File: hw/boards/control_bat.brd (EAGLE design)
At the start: 101.6 x 30.5 mm, 18 parts, among them U1 579-MCP1703T-3002ECB, U2 771-LPC824M201JDH20J, U3 888-XB24CZ7PIS-004

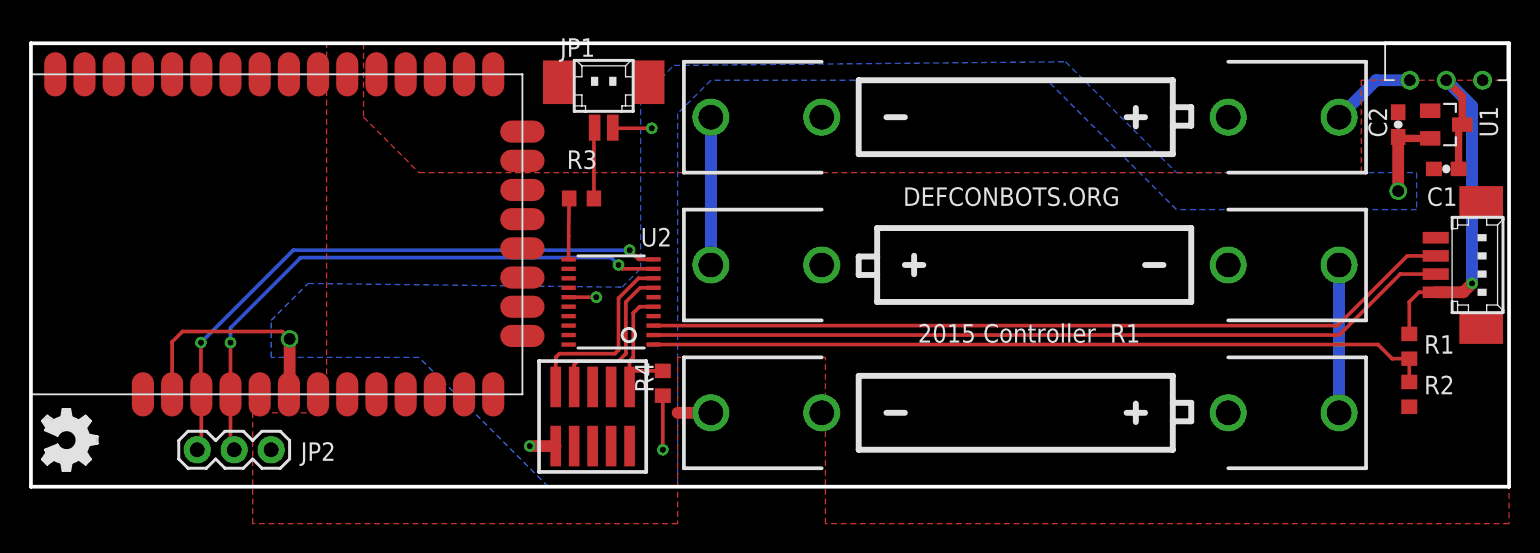
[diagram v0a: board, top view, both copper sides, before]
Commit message: Cleanup some routing. Fix some part numbers
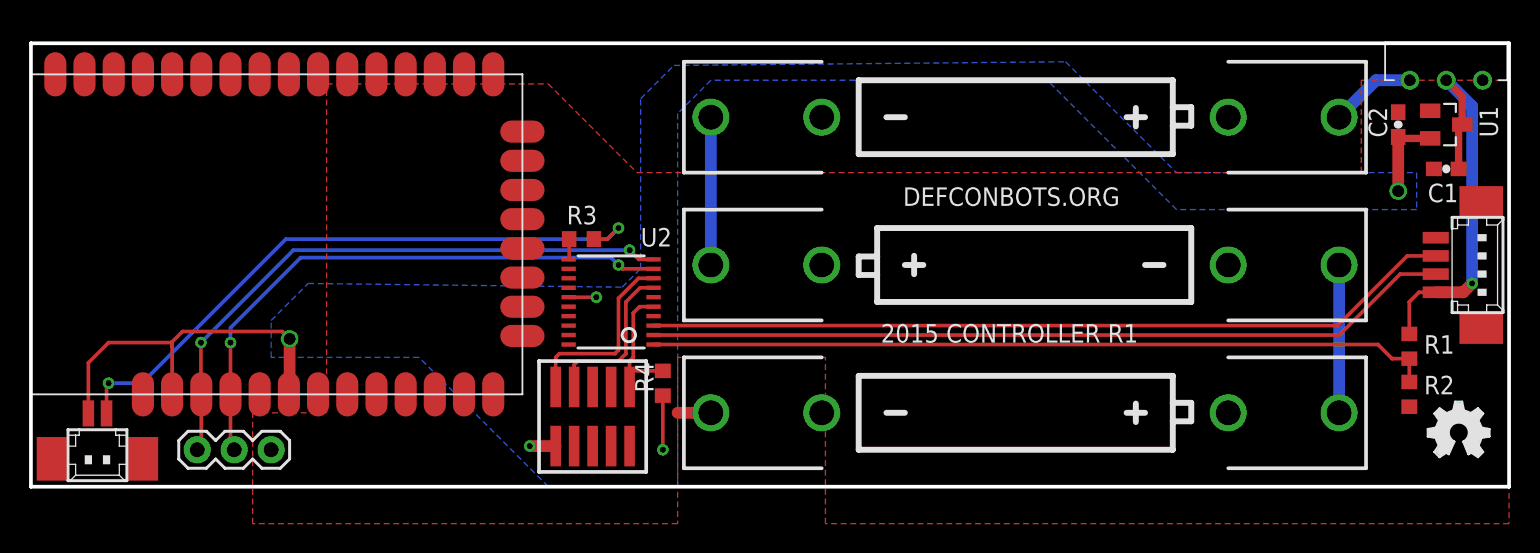
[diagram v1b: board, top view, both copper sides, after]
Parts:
- JP1: value 53398-02 -> 798-DF132P125V20
- JP2: value (none) -> 798-DF134P125V20; device SparkFun-Connectors:1X03 -> con-molex:53398-04
- JP4: value 798-DF134P125V20 -> (none); device con-molex:53398-04 -> SparkFun-Connectors:1X03
- moved LOGO1 95.3 mm to (96.0, 2.03), turned to 0 degrees
- moved JP2 88.5 mm to (99.1, 15.2), turned to 270 degrees
- moved JP4 88.5 mm to (11.4, 2.54), turned to 0 degrees
- moved JP1 42.6 mm to (4.57, 2.54), turned to 180 degrees
- moved R3 2.79 mm to (37.8, 17.0)
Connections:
- net GND: now also JP2.4, JP4.3; no longer JP2.3, JP4.4
- net RF_RX: now also JP4.1; no longer JP2.1
- net RF_TX: now also JP4.2; no longer JP2.2
- net RX: now also JP2.3; no longer JP4.3
- net TX: now also JP2.2; no longer JP4.2
- net VIN: now also JP2.1; no longer JP4.1
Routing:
- net N$4: track 4.91 -> 43.6 mm, vias 0 -> 2
- net +3V3: track 32.1 -> 39.2 mm, vias 6 -> 5
- net IR: track 4.19 -> 1.43 mm
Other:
- board text added: "2015 CONTROLLER R1"
- board text removed: "2015 Controller"
- board text removed: "R1"
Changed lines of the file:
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@@
 <wire x1="0" y1="30.48" x2="0" y2="0" width="0.254" layer="20"/>
 <text x="59.944" y="19.304" size="1.27" layer="21" font="vector" ratio="10">DEFCONBOTS.ORG</text>
-<text x="60.96" y="9.906" size="1.27" layer="21">2015 Controller</text>
-<text x="74.168" y="9.906" size="1.27" layer="21">R1</text>
+<text x="58.42" y="9.906" size="1.27" layer="21">2015 CONTROLLER R1</text>
 </plain>
 <attributes>
@@
 </element>
 <element name="C1" library="SparkFun-Passives" package="0603-CAP" value="C1608X5R1C106M080AB" x="97.282" y="21.844" smashed="yes" rot="R180">
-<attribute name="NAME" x="98.044" y="20.574" size="1.27" layer="25" font="vector" rot="R180"/>
+<attribute name="NAME" x="96.012" y="19.558" size="1.27" layer="25" font="vector"/>
 <attribute name="VALUE" x="98.298" y="22.987" size="0.4064" layer="27" font="vector" rot="R180"/>
 </element>
@@
 <attribute name="VALUE" x="95.123" y="23.876" size="0.4064" layer="27" font="vector" rot="R90"/>
 </element>
-<element name="JP4" library="con-molex" package="53398-04" value="798-DF134P125V20" x="99.06" y="15.24" smashed="yes" rot="R270">
+<element name="JP2" library="con-molex" package="53398-04" value="798-DF134P125V20" x="99.06" y="15.24" smashed="yes" rot="R270">
 <attribute name="OC_NEWARK" value="unknown" x="49.53" y="39.37" size="1.778" layer="27" rot="R270" display="off"/>
 <attribute name="MPN" value="" x="49.53" y="39.37" size="1.778" layer="27" rot="R270" display="off"/>
@@
 <attribute name="PROD_ID" value="BATT-08571" x="68.326" y="25.4" size="1.778" layer="27" rot="R180" display="off"/>
 </element>
-<element name="LOGO1" library="ohw-logo" package="OSHW_FILLX150_NOTEXT" value="OSHW_LOGO_FILLX0150-NT" x="0.762" y="5.334" smashed="yes" rot="R270"/>
+<element name="LOGO1" library="ohw-logo" package="OSHW_FILLX150_NOTEXT" value="OSHW_LOGO_FILLX0150-NT" x="96.012" y="2.032" smashed="yes"/>
 <element name="R1" library="rcl" package="R0603" value="71-CRCW0603-10K-E3" x="94.742" y="9.652" smashed="yes" rot="R90">
 <attribute name="NAME" x="95.758" y="9.144" size="1.27" layer="25"/>
@@
 <attribute name="VALUE" x="96.647" y="5.715" size="1.27" layer="27" rot="R90"/>
 </element>
-<element name="JP2" library="SparkFun-Connectors" package="1X03" value="" x="11.43" y="2.54" smashed="yes">
-<attribute name="NAME" x="18.542" y="1.778" size="1.27" layer="25" ratio="10"/>
+<element name="JP4" library="SparkFun-Connectors" package="1X03" value="" x="11.43" y="2.54" smashed="yes">
 <attribute name="VALUE" x="10.16" y="-0.635" size="1.27" layer="27"/>
 </element>
-<element name="R3" library="rcl" package="R0603" value="71-CRCW0603220RFKEB" x="37.846" y="19.812" smashed="yes">
-<attribute name="NAME" x="36.83" y="21.844" size="1.27" layer="25"/>
-<attribute name="VALUE" x="37.211" y="17.907" size="1.27" layer="27"/>
+<element name="R3" library="rcl" package="R0603" value="71-CRCW0603220RFKEB" x="37.846" y="17.018" smashed="yes">
+<attribute name="NAME" x="36.83" y="18.034" size="1.27" layer="25"/>
+<attribute name="VALUE" x="37.211" y="15.113" size="1.27" layer="27"/>
 </element>
 <element name="U2" library="torpedo" package="TSSOP20" value="771-LPC824M201JDH20J" x="39.878" y="12.7" smashed="yes" rot="R90">
 <attribute name="NAME" x="41.91" y="16.51" size="1.27" layer="25" ratio="18"/>
 </element>
-<element name="R4" library="rcl" package="R0603" value="71-CRCW0603-10K-E3" x="43.434" y="7.112" rot="R90"/>
-<element name="JP1" library="con-molex" package="53398-02" value="53398-02" x="39.37" y="27.178">
-<attribute name="OC_NEWARK" value="unknown" x="39.37" y="27.178" size="1.778" layer="27" display="off"/>
-<attribute name="MPN" value="" x="39.37" y="27.178" size="1.778" layer="27" display="off"/>
-<attribute name="MF" value="" x="39.37" y="27.178" size="1.778" layer="27" display="off"/>
-<attribute name="OC_FARNELL" value="unknown" x="39.37" y="27.178" size="1.778" layer="27" display="off"/>
+<element name="R4" library="rcl" package="R0603" value="71-CRCW0603-10K-E3" x="43.434" y="7.112" smashed="yes" rot="R90">
+<attribute name="NAME" x="42.799" y="6.477" size="1.27" layer="25" rot="R90"/>
+<attribute name="VALUE" x="45.339" y="6.477" size="1.27" layer="27" rot="R90"/>
+</element>
+<element name="JP1" library="con-molex" package="53398-02" value="798-DF132P125V20" x="4.572" y="2.54" smashed="yes" rot="R180">
+<attribute name="OC_NEWARK" value="unknown" x="4.572" y="2.54" size="1.778" layer="27" rot="R180" display="off"/>
+<attribute name="MPN" value="" x="4.572" y="2.54" size="1.778" layer="27" rot="R180" display="off"/>
+<attribute name="MF" value="" x="4.572" y="2.54" size="1.778" layer="27" rot="R180" display="off"/>
+<attribute name="OC_FARNELL" value="unknown" x="4.572" y="2.54" size="1.778" layer="27" rot="R180" display="off"/>
+<attribute name="VALUE" x="7.072" y="6.04" size="1.27" layer="27" rot="R180"/>
 </element>
 </elements>
@@
 <contactref element="C1" pad="2"/>
 <contactref element="C2" pad="2"/>
-<contactref element="JP4" pad="4"/>
+<contactref element="JP2" pad="4"/>
 <contactref element="JP3" pad="9"/>
 <contactref element="JP3" pad="5"/>
@@
 <contactref element="R2" pad="1"/>
 <polygon width="0.254" layer="1">
-<vertex x="20.32" y="30.48"/>
-<vertex x="22.86" y="30.48"/>
-<vertex x="22.86" y="25.4"/>
-<vertex x="26.67" y="21.59"/>
+<vertex x="20.32" y="27.686"/>
+<vertex x="35.56" y="27.686"/>
+<vertex x="41.656" y="21.59"/>
 <vertex x="91.44" y="21.59"/>
 <vertex x="91.44" y="27.94"/>
@@
 </polygon>
 <wire x1="46.736" y1="5.08" x2="44.45" y2="5.08" width="0.8128" layer="1"/>
-<contactref element="JP2" pad="3"/>
+<contactref element="JP4" pad="3"/>
 <contactref element="U2" pad="16"/>
 </signal>
@@
 <wire x1="36.9602" y1="13.025" x2="38.862" y2="13.025" width="0.254" layer="1"/>
 <via x="38.862" y="13.025" extent="1-16" drill="0.4064"/>
-<wire x1="9.7028" y1="6.35" x2="9.7028" y2="9.9568" width="0.254" layer="1"/>
+<wire x1="9.7028" y1="6.35" x2="9.7028" y2="9.652" width="0.254" layer="1"/>
+<wire x1="9.7028" y1="9.906" x2="9.7028" y2="9.9568" width="0.254" layer="1"/>
 <wire x1="9.7028" y1="9.9568" x2="10.414" y2="10.668" width="0.254" layer="1"/>
 <wire x1="10.414" y1="10.668" x2="17.272" y2="10.668" width="0.254" layer="1"/>
@@
 <via x="43.434" y="2.54" extent="1-16" drill="0.4064"/>
 <contactref element="JP1" pad="1"/>
-<wire x1="39.995" y1="24.678" x2="39.995" y2="24.638" width="0.254" layer="1"/>
-<wire x1="39.995" y1="24.638" x2="42.672" y2="24.638" width="0.254" layer="1"/>
-<via x="42.672" y="24.638" extent="1-16" drill="0.4064"/>
+<wire x1="3.947" y1="5.04" x2="3.947" y2="8.519" width="0.254" layer="1"/>
+<wire x1="3.947" y1="8.519" x2="5.334" y2="9.906" width="0.254" layer="1"/>
+<wire x1="5.334" y1="9.906" x2="9.7028" y2="9.906" width="0.254" layer="1"/>
+<wire x1="9.7028" y1="9.906" x2="9.7028" y2="9.652" width="0.254" layer="1"/>
 </signal>
 <signal name="VIN">
 <contactref element="U1" pad="3"/>
 <contactref element="C1" pad="1"/>
-<contactref element="JP4" pad="1"/>
+<contactref element="JP2" pad="1"/>
 <contactref element="R1" pad="2"/>
 <contactref element="S1" pad="P$2"/>
@@
 </signal>
 <signal name="TX">
-<contactref element="JP4" pad="2"/>
+<contactref element="JP2" pad="2"/>
 <wire x1="96.56" y1="14.615" x2="94.117" y2="14.615" width="0.254" layer="1"/>
 <wire x1="94.117" y1="14.615" x2="89.927" y2="10.425" width="0.254" layer="1"/>
@@
 </signal>
 <signal name="RX">
-<contactref element="JP4" pad="3"/>
+<contactref element="JP2" pad="3"/>
 <wire x1="96.56" y1="15.865" x2="94.605" y2="15.865" width="0.254" layer="1"/>
 <wire x1="94.605" y1="15.865" x2="89.815" y2="11.075" width="0.254" layer="1"/>
@@
 <via x="13.716" y="9.906" extent="1-16" drill="0.4064"/>
 <wire x1="13.716" y1="9.906" x2="13.716" y2="6.35" width="0.254" layer="1"/>
-<contactref element="JP2" pad="2"/>
+<contactref element="JP4" pad="2"/>
 <wire x1="13.716" y1="6.35" x2="13.716" y2="2.794" width="0.254" layer="1"/>
 <wire x1="13.716" y1="2.794" x2="13.97" y2="2.54" width="0.254" layer="1"/>
@@
 <wire x1="11.684" y1="9.906" x2="11.684" y2="6.3754" width="0.254" layer="1"/>
 <wire x1="11.684" y1="6.3754" x2="11.7094" y2="6.35" width="0.254" layer="1"/>
-<contactref element="JP2" pad="1"/>
+<contactref element="JP4" pad="1"/>
 <wire x1="11.7094" y1="6.35" x2="11.7094" y2="2.8194" width="0.254" layer="1"/>
 <wire x1="11.7094" y1="2.8194" x2="11.43" y2="2.54" width="0.254" layer="1"/>
@@
 <contactref element="R3" pad="2"/>
 <contactref element="JP1" pad="2"/>
-<wire x1="38.745" y1="24.678" x2="38.696" y2="24.678" width="0.254" layer="1"/>
-<wire x1="38.696" y1="24.678" x2="38.696" y2="19.812" width="0.254" layer="1"/>
+<wire x1="38.696" y1="17.018" x2="39.624" y2="17.018" width="0.254" layer="1"/>
+<wire x1="39.624" y1="17.018" x2="40.386" y2="17.78" width="0.254" layer="1"/>
+<via x="40.386" y="17.78" extent="1-16" drill="0.4064"/>
+<wire x1="40.386" y1="17.78" x2="39.624" y2="17.018" width="0.254" layer="16"/>
+<wire x1="39.624" y1="17.018" x2="17.526" y2="17.018" width="0.254" layer="16"/>
+<wire x1="17.526" y1="17.018" x2="7.62" y2="7.112" width="0.254" layer="16"/>
+<wire x1="7.62" y1="7.112" x2="5.334" y2="7.112" width="0.254" layer="16"/>
+<via x="5.334" y="7.112" extent="1-16" drill="0.4064"/>
+<wire x1="5.334" y1="7.112" x2="5.197" y2="6.975" width="0.254" layer="1"/>
+<wire x1="5.197" y1="6.975" x2="5.197" y2="5.04" width="0.254" layer="1"/>
 </signal>
 <signal name="IR">
 <contactref element="R3" pad="1"/>
 <contactref element="U2" pad="11"/>
-<wire x1="36.996" y1="19.812" x2="36.9602" y2="17.2362" width="0.254" layer="1"/>
-<wire x1="36.9602" y1="17.2362" x2="36.9602" y2="15.625" width="0.254" layer="1"/>
+<wire x1="36.9602" y1="15.625" x2="36.996" y2="15.625" width="0.254" layer="1"/>
+<wire x1="36.996" y1="15.625" x2="36.996" y2="17.018" width="0.254" layer="1"/>
 </signal>
 </signals>
